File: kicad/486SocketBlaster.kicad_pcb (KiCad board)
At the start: 2 copper layers, 47.5 x 51.7 mm, 11 parts, among them U3 VoltageRegulator

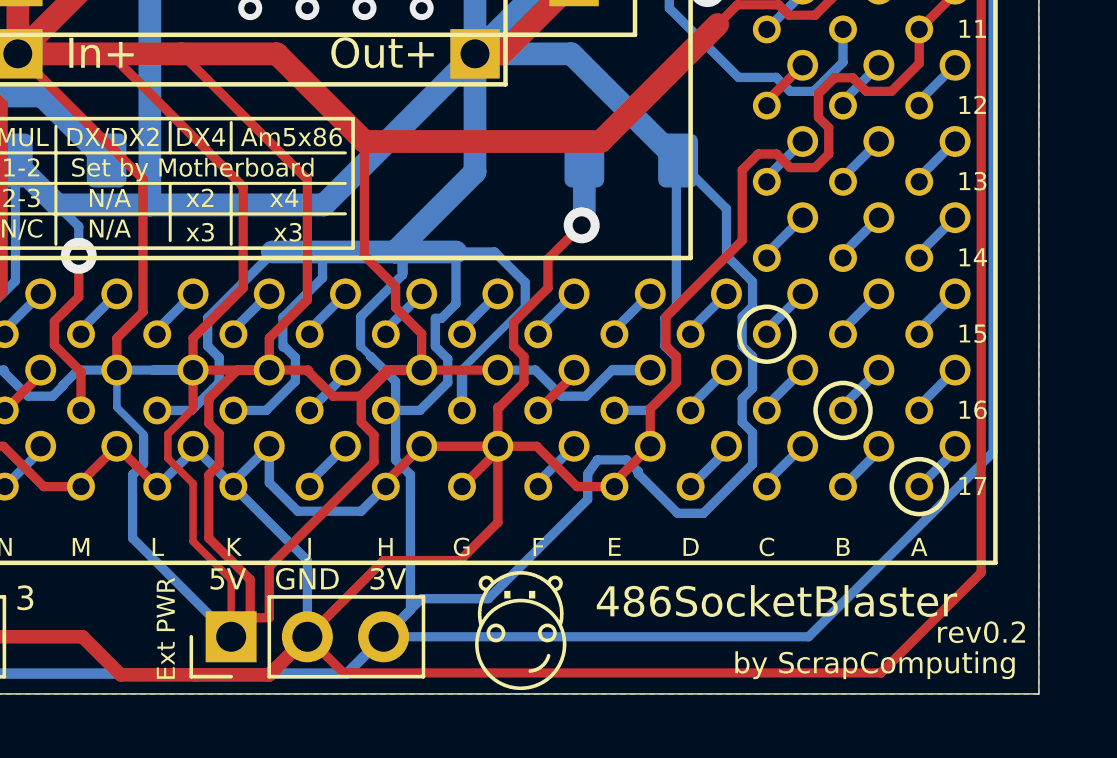
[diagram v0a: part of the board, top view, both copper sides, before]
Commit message: Fixed CPUMUL multipliers table and changed capacitor values to 10uF
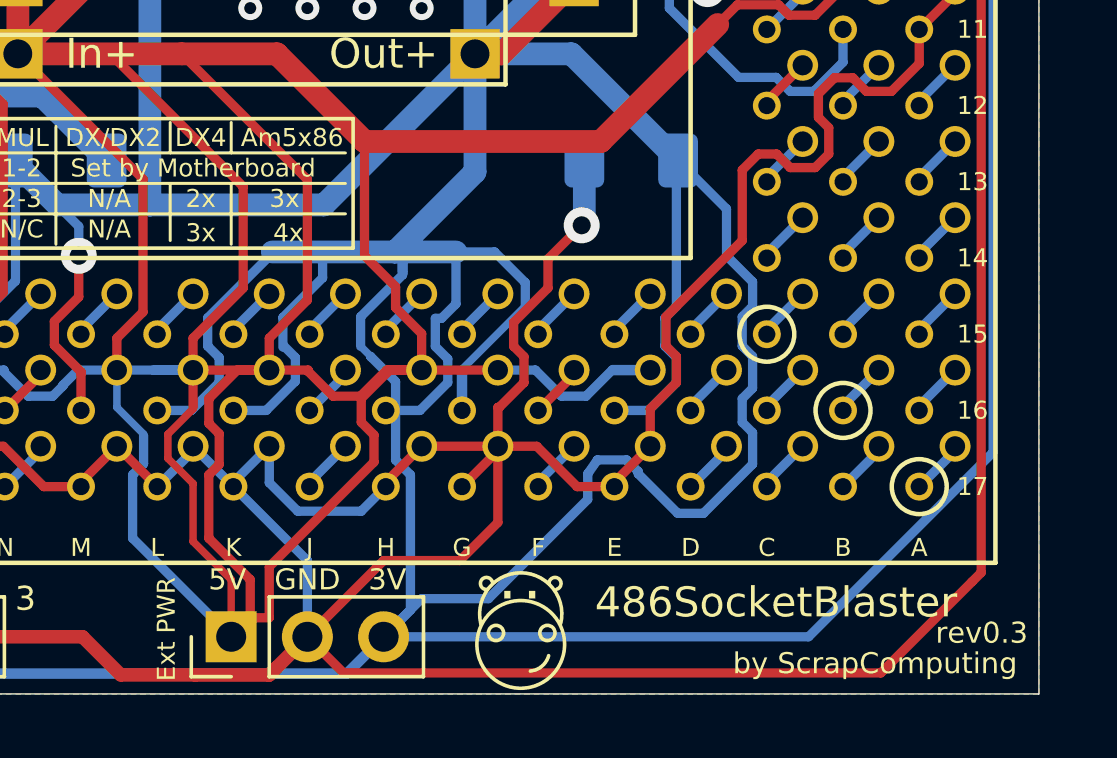
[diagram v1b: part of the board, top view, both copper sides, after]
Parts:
- 10uF (x4): renamed from 0.1uF; value 0.1uF -> 10uF
- 10uF: renamed from 1uF; value 1uF -> 10uF
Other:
- board text added: "2x"
- board text added: "3x"
- board text added: "4x"
- board text added: "rev0.3"
- board text removed: "rev0.2"
- board text removed: "x2"
- board text removed: "x3"
- board text removed: "x4"
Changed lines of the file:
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@@
   (page A4)
   (layers
-    (0 F.Cu signal)
-    (31 B.Cu signal)
+    (0 F.Cu signal hide)
+    (31 B.Cu signal hide)
     (32 B.Adhes user)
     (33 F.Adhes user)
@@
     (tags "capacitor handsolder")
     (attr smd)
-    (fp_text reference 0.1uF (at -0.635 -1.905) (layer B.SilkS)
+    (fp_text reference 10uF (at -0.635 -1.905) (layer B.SilkS)
       (effects (font (size 1 1) (thickness 0.15)) (justify mirror))
     )
-    (fp_text value 0.1uF (at 0 -1.85) (layer B.Fab)
+    (fp_text value 10uF (at 0 -1.85) (layer B.Fab)
       (effects (font (size 1 1) (thickness 0.15)) (justify mirror))
     )
@@
     (tags "capacitor handsolder")
     (attr smd)
-    (fp_text reference 0.1uF (at 0 1.85) (layer B.SilkS)
+    (fp_text reference 10uF (at 0 1.85) (layer B.SilkS)
       (effects (font (size 1 1) (thickness 0.15)) (justify mirror))
     )
-    (fp_text value 0.1uF (at 0 -1.85) (layer B.Fab)
+    (fp_text value 10uF (at 0 -1.85) (layer B.Fab)
       (effects (font (size 1 1) (thickness 0.15)) (justify mirror))
     )
@@
     (tags "capacitor handsolder")
     (attr smd)
-    (fp_text reference 0.1uF (at 0 1.85) (layer B.SilkS)
+    (fp_text reference 10uF (at 0 1.85) (layer B.SilkS)
       (effects (font (size 1 1) (thickness 0.15)) (justify mirror))
     )
-    (fp_text value 0.1uF (at 0 -1.85) (layer B.Fab)
+    (fp_text value 10uF (at 0 -1.85) (layer B.Fab)
       (effects (font (size 1 1) (thickness 0.15)) (justify mirror))
     )
@@
     (tags "capacitor handsolder")
     (attr smd)
-    (fp_text reference 0.1uF (at 0 1.85) (layer B.SilkS)
+    (fp_text reference 10uF (at 0 1.85) (layer B.SilkS)
       (effects (font (size 1 1) (thickness 0.15)) (justify mirror))
     )
-    (fp_text value 0.1uF (at 0 -1.85) (layer B.Fab)
+    (fp_text value 10uF (at 0 -1.85) (layer B.Fab)
       (effects (font (size 1 1) (thickness 0.15)) (justify mirror))
     )
@@
     (descr "C, Rect series, Radial, pin pitch=5.00mm, , length*width=7*3.5mm^2, Capacitor")
     (tags "C Rect series Radial pin pitch 5.00mm  length 7mm width 3.5mm Capacitor")
-    (fp_text reference 1uF (at 2.5 0 270) (layer B.SilkS)
-      (effects (font (size 1 1) (thickness 0.15)) (justify mirror))
-    )
-    (fp_text value 1uF (at 2.54 -1.27 270) (layer B.Fab)
+    (fp_text reference 10uF (at 2.5 0 270) (layer B.SilkS)
+      (effects (font (size 0.8 0.8) (thickness 0.15)) (justify mirror))
+    )
+    (fp_text value 10uF (at 2.54 -1.27 270) (layer B.Fab)
       (effects (font (size 1 1) (thickness 0.15)) (justify mirror))
     )
@@
     (fp_line (start -1 -1.75) (end 6 -1.75) (layer B.Fab) (width 0.1))
     (fp_line (start -1 1.75) (end -1 -1.75) (layer B.Fab) (width 0.1))
-    (fp_text user %R (at 2.5 0 270) (layer B.Fab)
-      (effects (font (size 1 1) (thickness 0.15)) (justify mirror))
+    (fp_text user 10uF (at 2.5 0 270) (layer B.Fab)
+      (effects (font (size 0.8 0.8) (thickness 0.15)) (justify mirror))
     )
     (pad 2 thru_hole circle (at 5 0 90) (size 1.6 1.6) (drill 0.8) (layers *.Cu *.Mask)
@@
     (effects (font (size 0.8 0.8) (thickness 0.13)) (justify mirror))
   )
-  (gr_text rev0.2 (at 143.129 78.613) (layer F.SilkS)
+  (gr_text rev0.3 (at 143.129 78.613) (layer F.SilkS)
     (effects (font (size 0.7 0.7) (thickness 0.11)))
   )
@@
   (gr_line (start 116.078 62.611) (end 116.078 61.595) (layer F.SilkS) (width 0.1))
   (gr_line (start 118.11 62.611) (end 118.11 61.595) (layer F.SilkS) (width 0.1))
-  (gr_text x3 (at 120.015 65.278) (layer F.SilkS)
+  (gr_text 4x (at 120.015 65.278) (layer F.SilkS)
     (effects (font (size 0.6 0.6) (thickness 0.11)))
   )
@@
   (gr_line (start 112.268 65.659) (end 112.268 61.722) (layer F.SilkS) (width 0.1))
   (gr_line (start 108.712 62.611) (end 121.92 62.611) (layer F.SilkS) (width 0.1))
-  (gr_text x4 (at 119.888 64.135) (layer F.SilkS)
+  (gr_text 3x (at 119.888 64.135) (layer F.SilkS)
     (effects (font (size 0.6 0.6) (thickness 0.11)))
   )
-  (gr_text x2 (at 117.094 64.135) (layer F.SilkS)
+  (gr_text 2x (at 117.094 64.135) (layer F.SilkS)
     (effects (font (size 0.6 0.6) (thickness 0.11)))
   )
@@
     (effects (font (size 0.6 0.6) (thickness 0.11)))
   )
-  (gr_text x3 (at 117.094 65.278) (layer F.SilkS)
+  (gr_text 3x (at 117.094 65.278) (layer F.SilkS)
     (effects (font (size 0.6 0.6) (thickness 0.11)))
   )

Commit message: Larger holes (and pads) for 0.55mm female pin headers.
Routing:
- net Net-(C1-Pad1): track 589.2 -> 609.9 mm
- net GND: track 440.3 -> 456.2 mm
- net Net-(Bot1-PadB11): track 316.9 -> 330.8 mm
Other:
- board text added: "rev0.4"
- board text removed: "rev0.3"

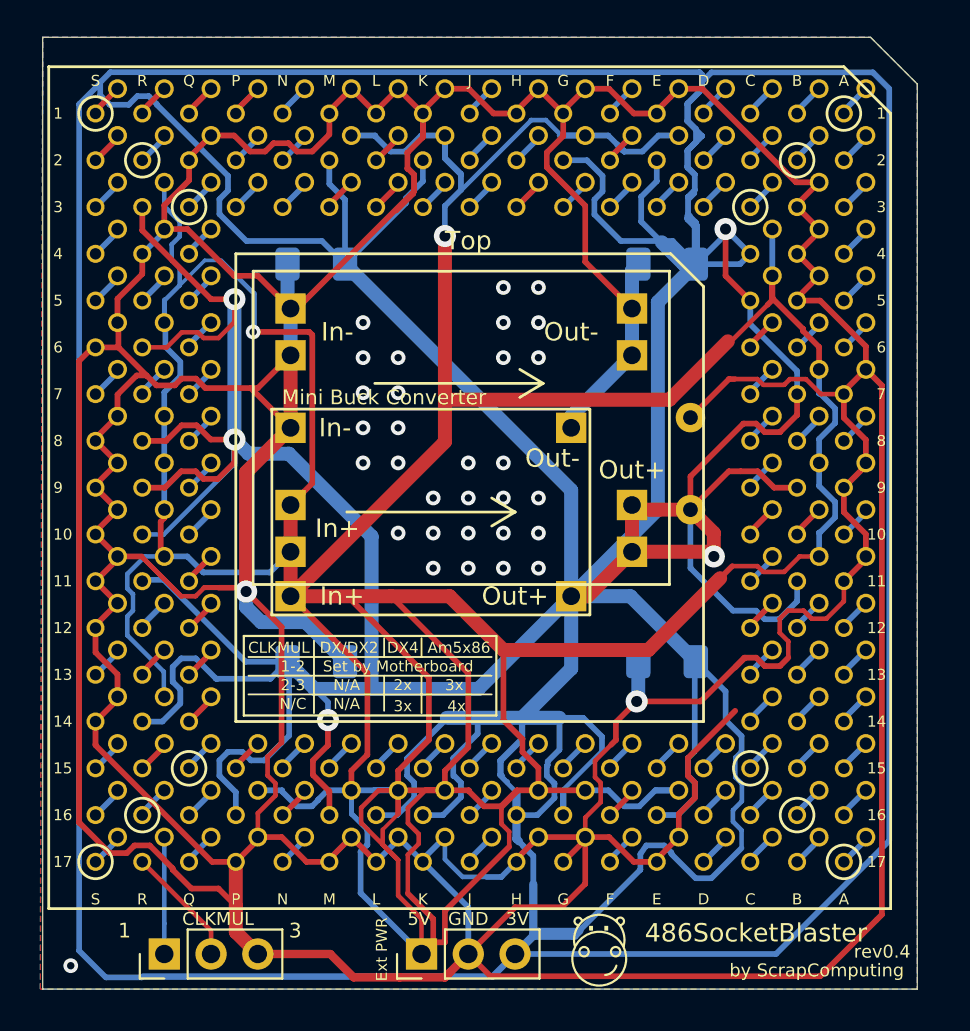
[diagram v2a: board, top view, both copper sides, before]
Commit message: Rev 0.5: Add WB/WT header and fix CLKMUL table silkscreen for am5x86
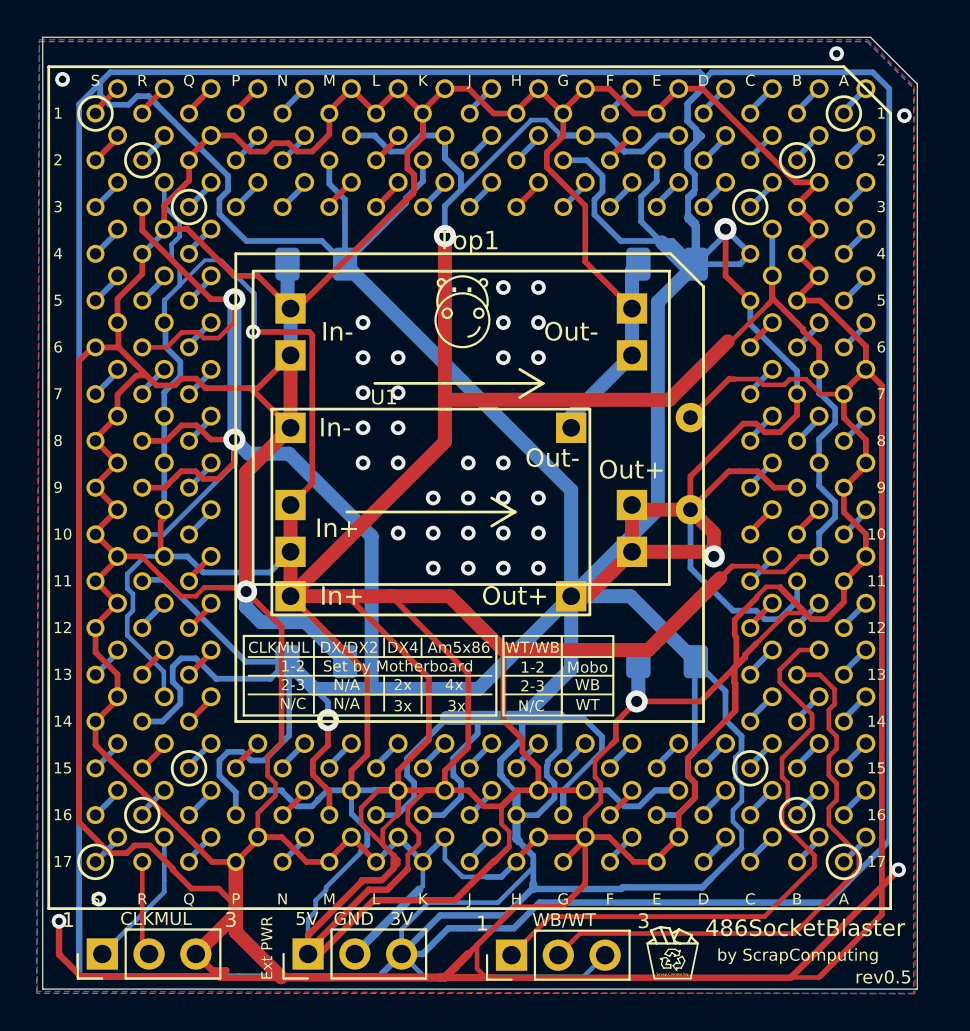
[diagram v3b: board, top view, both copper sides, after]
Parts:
- removed Mini Buck Converter: VoltageRegulator, 486pga:VoltageRegulator2
- added J1: Conn_01x03, Connector_PinHeader_2.54mm:PinHeader_1x03_P2.54mm_Vertical, F.Cu at (123.0, 78.8)
- added U1: VoltageRegulator, 486pga:VoltageRegulator2, F.Cu at (111.0, 56.9)
- moved ExtPwr1 6.16 mm to (112.0, 78.7)
- moved CLKMUL 3.37 mm to (100.8, 78.7)
- renumbered 10uF to C1, 10uF to C2, 10uF to C3, 10uF to C4, 10uF to C5, Top to Top1
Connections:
- Top1 pad B13: Net-(Bot1-PadB13) -> Net-(J1-Pad2)
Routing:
- net GND: track 456.2 -> 542.6 mm, vias 33 -> 38
- net Net-(Bot1-PadB13): track 1.84 -> 34.6 mm
- net Net-(J1-Pad2): track 0.00 -> 32.0 mm
- net Net-(C1-Pad1): track 609.9 -> 629.0 mm
- net Net-(Bot1-PadB11): track 330.8 -> 338.5 mm
- net Net-(CLKMUL1-Pad2): track 6.55 -> 5.16 mm
- net Net-(Bot1-PadR17): track 6.50 -> 7.89 mm
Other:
- board text added: "10uF"
- board text added: "1uF"
- board text added: "Mobo"
- board text added: "Scrap Computing"
- board text added: "WB"
- board text added: "WB/WT"
- board text added: "WT"
- board text added: "WT/WB"
- board text added: "rev0.5"
- board text removed: "rev0.4"
